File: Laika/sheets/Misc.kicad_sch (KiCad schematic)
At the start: 27 parts, among them Q1 MMBT5551, Q2 2N7002, SW1 SW_Push, SW2 SW_Push, SW3 JS202011JAQN

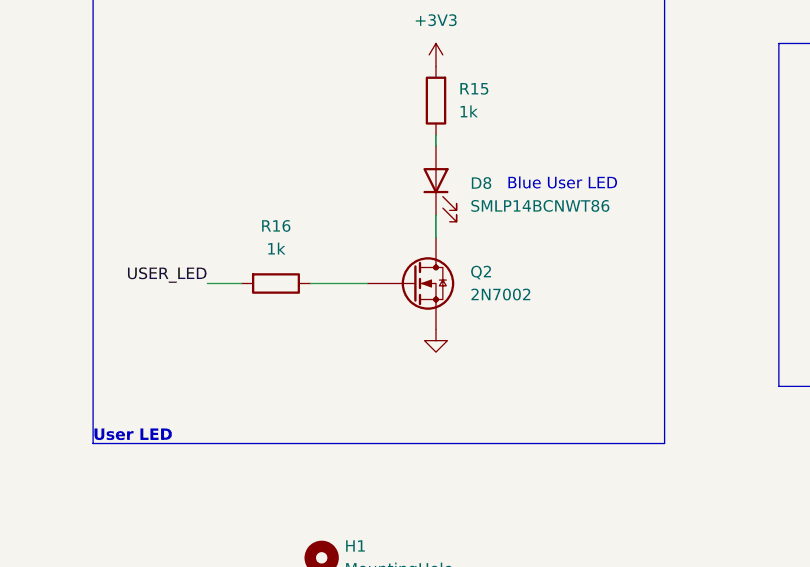
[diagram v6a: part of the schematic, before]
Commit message: Replace generic NMOS symbol with 2N7002
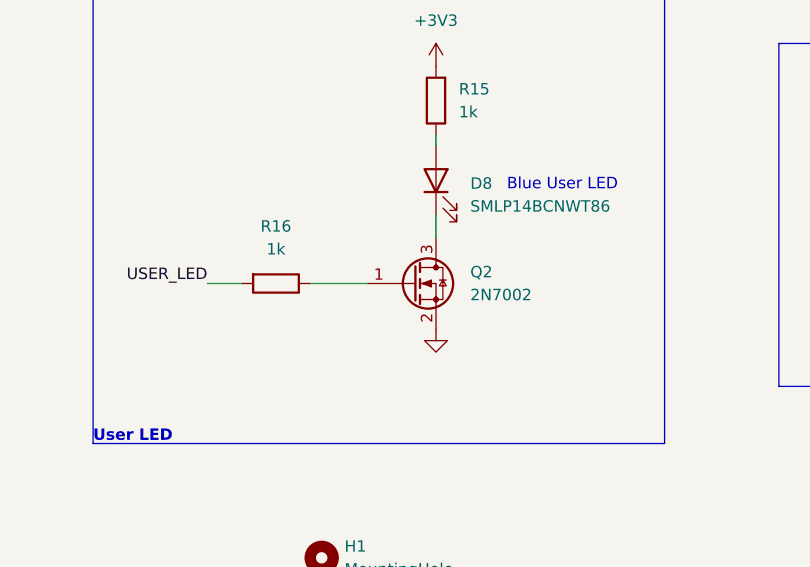
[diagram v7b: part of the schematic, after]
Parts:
- Q2: footprint Package_TO_SOT_SMD:SOT-23-3 -> Package_TO_SOT_SMD:SOT-23; symbol Device:Q_NMOS -> Transistor_FET:2N7002
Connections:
- net GND: now also Q2.2 (S); no longer Q2.S
- net at D8.1 (K): now also Q2.3 (D); no longer Q2.D
- net at R16.1: now also Q2.1 (G); no longer Q2.G
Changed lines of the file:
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@@
 	)
 	(symbol
-		(lib_id "Device:Q_NMOS")
+		(lib_id "Transistor_FET:2N7002")
 		(at 149.86 147.32 0)
 		(unit 1)
@@
 			)
 		)
-		(property "Footprint" "Package_TO_SOT_SMD:SOT-23-3"
-			(at 154.94 144.78 0)
+		(property "Footprint" "Package_TO_SOT_SMD:SOT-23"
+			(at 154.94 149.225 0)
+			(effects
+				(font
+					(size 1.27 1.27)
+					(italic yes)
+				)
+				(justify left)
+				(hide yes)
+			)
+		)
+		(property "Datasheet" "https://www.onsemi.com/pub/Collateral/NDS7002A-D.PDF"
+			(at 154.94 151.13 0)
 			(effects
 				(font
 					(size 1.27 1.27)
 				)
+				(justify left)
 				(hide yes)
 			)
 		)
-		(property "Datasheet" "https://www.onsemi.com/download/data-sheet/pdf/nds7002a-d.pdf"
-			(at 149.86 147.32 0)
-			(effects
-				(font
-					(size 1.27 1.27)
-				)
-				(hide yes)
-			)
-		)
-		(property "Description" "N-MOSFET transistor"
+		(property "Description" "0.115A Id, 60V Vds, N-Channel MOSFET, SOT-23"
 			(at 149.86 147.32 0)
 			(effects
@@
 			)
 		)
-		(pin "D"
+		(pin "1"
 		)
-		(pin "S"
+		(pin "2"
 		)
-		(pin "G"
+		(pin "3"
 		)
 		(instances

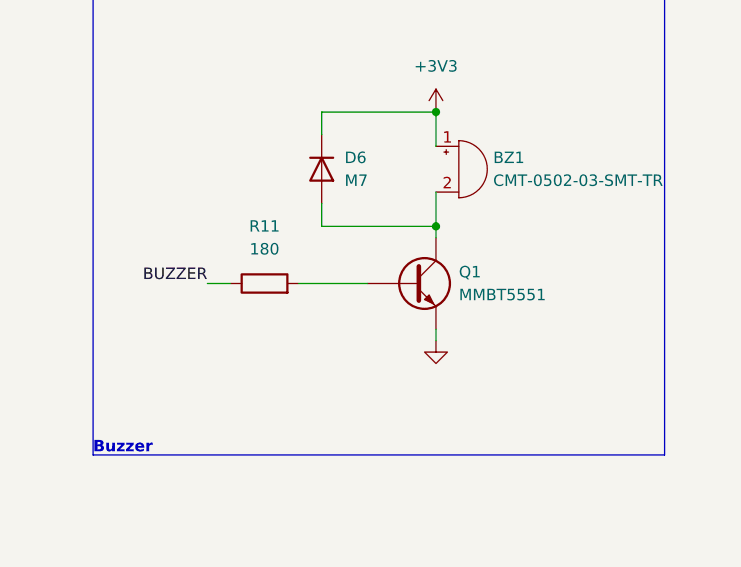
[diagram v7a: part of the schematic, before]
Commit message: Replace generic NPN with MMBT5551 symbol
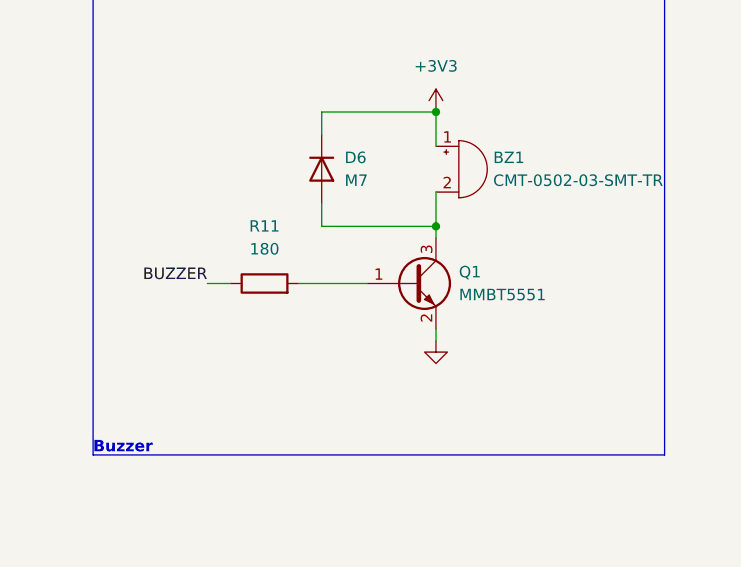
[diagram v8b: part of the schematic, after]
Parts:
- Q1: symbol Device:Q_NPN -> Transistor_BJT:MMBT5551L
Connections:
- net GND: now also Q1.2 (E); no longer Q1.E
- net at R11.2: now also Q1.1 (B); no longer Q1.B
- net at BZ1.2 (-), D6.2 (A): now also Q1.3 (C); no longer Q1.C
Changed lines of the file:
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@@
 	)
 	(symbol
-		(lib_id "Device:Q_NPN")
+		(lib_id "Transistor_BJT:MMBT5551L")
 		(at 226.06 82.55 0)
 		(unit 1)
@@
 		)
 		(property "Footprint" "Package_TO_SOT_SMD:SOT-23"
-			(at 231.14 80.01 0)
+			(at 231.14 84.455 0)
 			(effects
 				(font
 					(size 1.27 1.27)
+					(italic yes)
 				)
+				(justify left)
 				(hide yes)
 			)
 		)
-		(property "Datasheet" "https://diotec.com/request/datasheet/mmbt5551.pdf"
+		(property "Datasheet" "www.onsemi.com/pub/Collateral/MMBT5550LT1-D.PDF"
 			(at 226.06 82.55 0)
 			(effects
@@
 					(size 1.27 1.27)
 				)
+				(justify left)
 				(hide yes)
 			)
 		)
-		(property "Description" "NPN bipolar junction transistor"
+		(property "Description" "0.6A Ic, 160V Vce, NPN Transistor, SOT-23"
 			(at 226.06 82.55 0)
 			(effects
@@
 			)
 		)
-		(pin "B"
+		(pin "2"
 		)
-		(pin "C"
+		(pin "1"
 		)
-		(pin "E"
+		(pin "3"
 		)
 		(instances
